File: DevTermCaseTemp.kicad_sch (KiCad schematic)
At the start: 87 parts, among them J1 USB_A, J2 EXT_miniPCIe, J3 USB_A, J4 USB_B_Micro, J5 Conn_01x02, J6 Conn_01x04, J7 DevTermSpeaker, J8 DevTermSpeaker, J9 Conn_02x22_Odd_Even, SW1 SW_DIP_x02, SW2 SW_SPDT, U1 GL850G, U10 4052, U11 4052, U12 TXS0102DCT, U13 DevTermFan3505, U2 SY6280, U3 SY6280, U4 DS1307+, U5 MCP23008-xSS, U6 CH340N, U7 4052, U8 4052, U9 gp7101, Y1 12MHz, Y2 32.768KHz

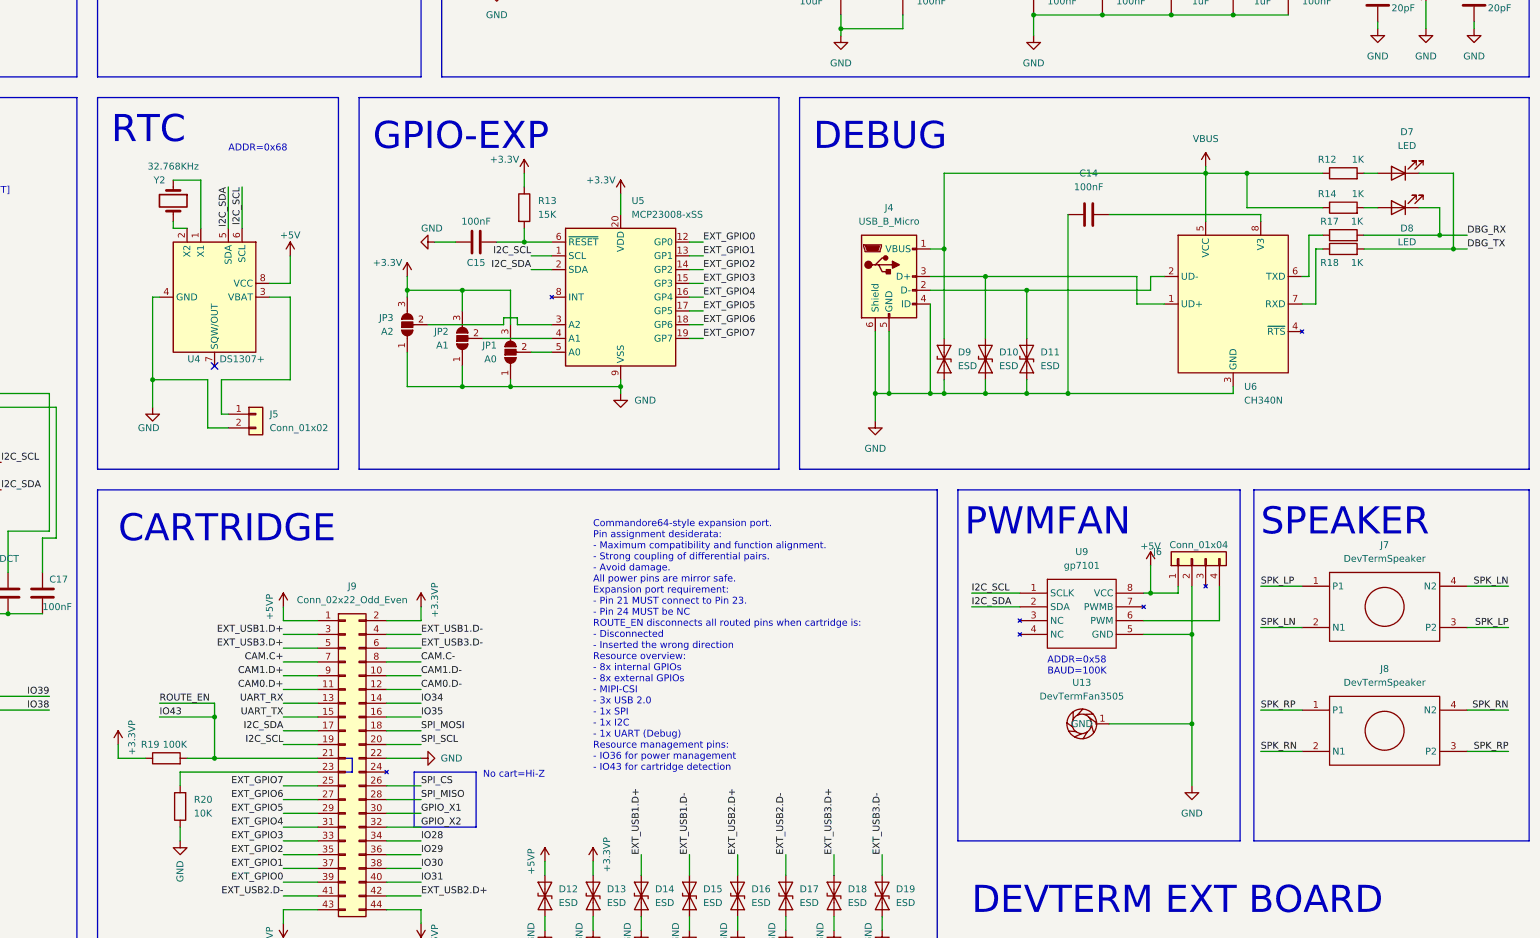
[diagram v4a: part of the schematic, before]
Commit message: Schematic:  - Replace GP7101 with EMC2301 and add support for directly driven fan  - Replace 3505/3507 fan with either a CUI Devices CBM-35CF or stock DevTerm fan  - Use correct footprint for MCP23008
Board:
 - Overhaul MIPI CSI line to match impedance and enhance EMC
 - Route new fan component
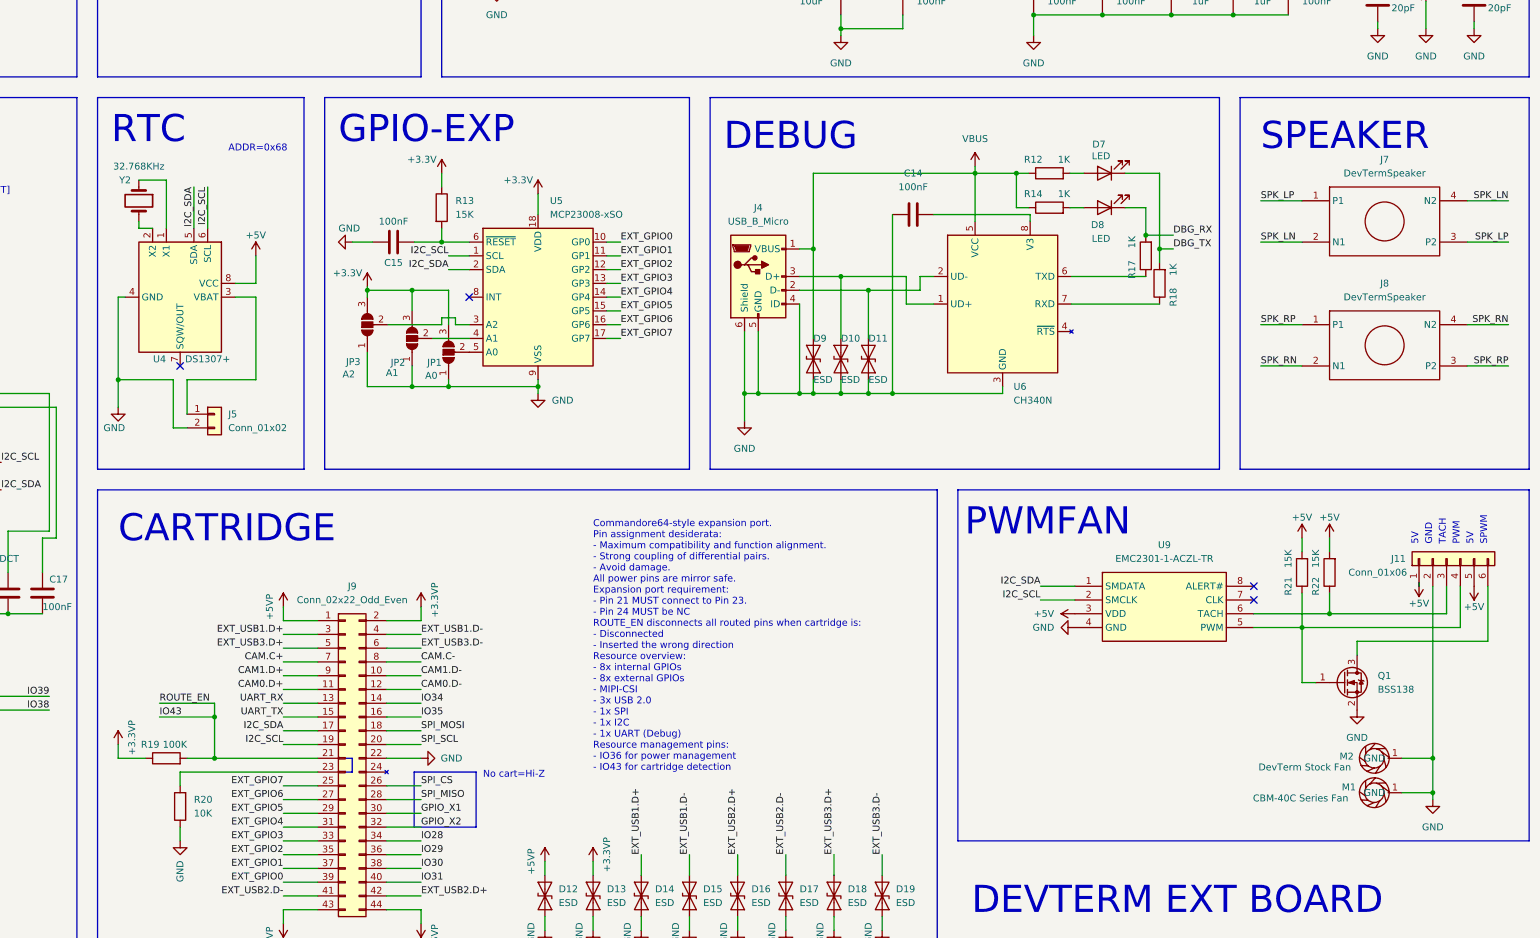
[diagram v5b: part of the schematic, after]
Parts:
- removed J6: Conn_01x04, Connector_PinSocket_2.00mm:PinSocket_1x04_P2.00mm_Vertical, symbol Connector_Generic:Conn_01x04
- removed U5: MCP23008-xSS, Package_SO:SOIC-20W_7.5x12.8mm_P1.27mm, symbol Interface_Expansion:MCP23008-xSS
- removed U9: gp7101, Package_SO:SOP-8_3.9x4.9mm_P1.27mm, symbol gp7101:gp7101
- added J11: Conn_01x06, Connector_PinHeader_2.00mm:PinHeader_1x06_P2.00mm_Horizontal, symbol Connector_Generic:Conn_01x06
- added M2: DevTerm Stock Fan, devterm-ext-outline:DevTerm-Stock-Fan, symbol devterm_symbols:DevTermFan3505
- added Q1: BSS138, Package_TO_SOT_SMD:SOT-23, symbol Transistor_FET:BSS138
- added R21, R22: 15K, Resistor_SMD:R_0805_2012Metric, symbol Device:R
- added U5: MCP23008-xSO, Package_SO:SOIC-18W_7.5x11.6mm_P1.27mm, symbol Interface_Expansion:MCP23008-xSO
- added U9: EMC2301-1-ACZL-TR, SOP65P490X110-8N, symbol EMC2301-1-ACZL-TR:EMC2301-1-ACZL-TR
- M1: renamed from U13; value DevTermFan3505 -> CBM-40C Series Fan; footprint devterm-ext-outline:turbo_fan_3505 -> devterm-ext-outline:CBM-40C-Series-Fan
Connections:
- net +3.3V: now also U5.18 (VDD)
- net +5V: now also J11.1 (Pin_1), J11.5 (Pin_5), R21.2, R22.2, U9.3 (VDD)
- net EXT_GPIO0: now also U5.10 (GP0)
- net EXT_GPIO1: now also U5.11 (GP1)
- net EXT_GPIO2: now also U5.12 (GP2)
- net EXT_GPIO3: now also U5.13 (GP3)
- net EXT_GPIO4: now also U5.14 (GP4)
- net EXT_GPIO5: now also U5.15 (GP5)
- net EXT_GPIO6: now also U5.16 (GP6)
- net EXT_GPIO7: now also U5.17 (GP7)
- net GND: now also J11.2 (Pin_2), M2.1 (GND), Q1.2 (S), U5.9 (VSS), U9.4 (GND)
- net I2C_SCL: now also U5.1 (SCL), U9.2 (SMCLK)
- net I2C_SDA: now also U5.2 (SDA), U9.1 (SMDATA)
- net at JP1.2 (C): now also U5.5 (A0)
- net at C15.2, R13.2: now also U5.6 (~{RESET})
- net at JP2.2 (C): now also U5.4 (A1)
- net at JP3.2 (C): now also U5.3 (A2)
- new net: J11.4 (Pin_4), Q1.1 (G), R21.1, U9.5 (PWM)
- new net: J11.3 (Pin_3), R22.1, U9.6 (TACH)
- new net: J11.6 (Pin_6), Q1.3 (D)
- no-connect marks 1 -> 4
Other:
- note added: "5V"
- note added: "GND"
- note added: "PWM"
- note added: "SPWM"
- note added: "TACH"
- note removed: "ADDR=0x58 BAUD=100K"
- moved on the sheet: C14, C15, D10, D11, D7, D8, D9, J4, J5, J7, J8, JP1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

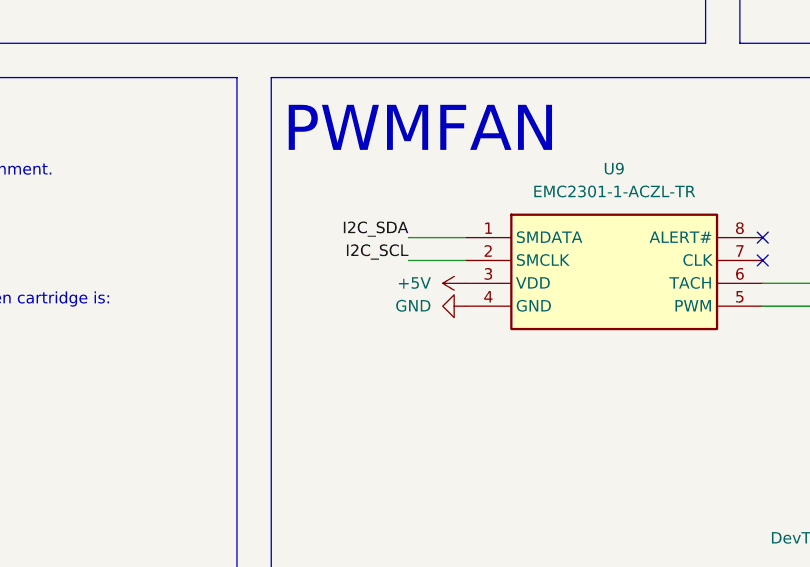
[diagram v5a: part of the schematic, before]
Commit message: Fix supply of EMC2301, add serial number field
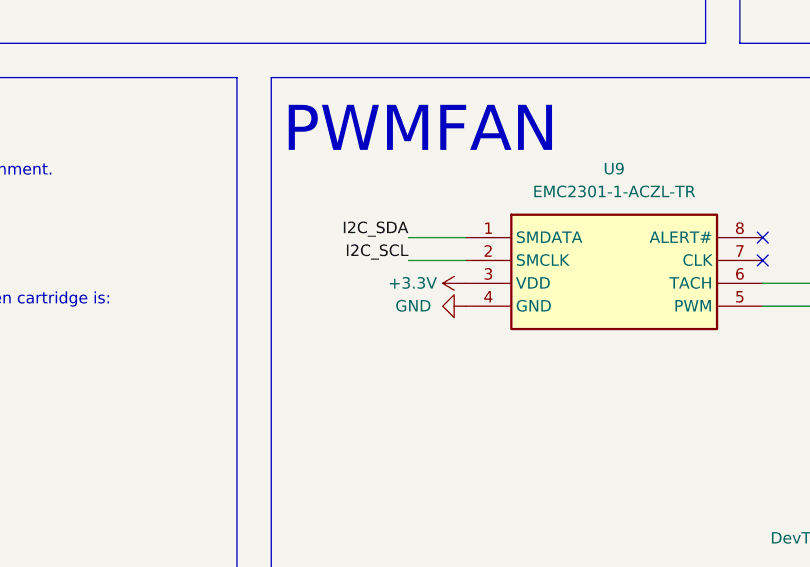
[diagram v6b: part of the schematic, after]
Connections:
- net +3.3V: now also U9.3 (VDD)
- net +5V: no longer U9.3 (VDD)
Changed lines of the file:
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@@
-    )
-  )
-  (symbol (lib_id "power:+5V") (at 321.31 208.28 90) (unit 1)
-    (in_bom yes) (on_board yes) (dnp no)
-    (property "Reference" "#PWR073" (at 325.12 208.28 0)
-      (effects (font (size 1.27 1.27)) hide)
-    )
-    (property "Value" "+5V" (at 315.595 208.28 90)
-      (effects (font (size 1.27 1.27)))
-    )
-    (property "Footprint" "" (at 321.31 208.28 0)
-      (effects (font (size 1.27 1.27)) hide)
-    )
-    (property "Datasheet" "" (at 321.31 208.28 0)
-      (effects (font (size 1.27 1.27)) hide)
-    )
-    (pin "1")
-    (instances
-      (project "DevTermCaseTemp"
-        (path "/92520c5a-b04b-416c-be0c-8c1bc8fc98c1"
-          (reference "#PWR073") (unit 1)
-        )
-      )
     )
   )
@@
         )
       )
+    )
+  )
+  (symbol (lib_id "power:+3.3V") (at 321.31 208.28 90) (unit 1)
+    (in_bom yes) (on_board yes) (dnp no)
+    (property "Reference" "#PWR073" (at 325.12 208.28 0)
+      (effects (font (size 1.27 1.27)) hide)
+    )
+    (property "Value" "+3.3V" (at 318.135 208.28 90)
+      (effects (font (size 1.27 1.27)) (justify left))
+    )
+    (property "Footprint" "" (at 321.31 208.28 0)
+      (effects (font (size 1.27 1.27)) hide)
+    )
+    (property "Datasheet" "" (at 321.31 208.28 0)
+      (effects (font (size 1.27 1.27)) hide)
+    )
+    (pin "1")
+    (instances
+      (project "DevTermCaseTemp"
+        (path "/92520c5a-b04b-416c-be0c-8c1bc8fc98c1"
+          (reference "#PWR073") (unit 1)
+        )
+      )
